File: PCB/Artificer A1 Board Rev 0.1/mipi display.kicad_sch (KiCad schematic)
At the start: 2 parts

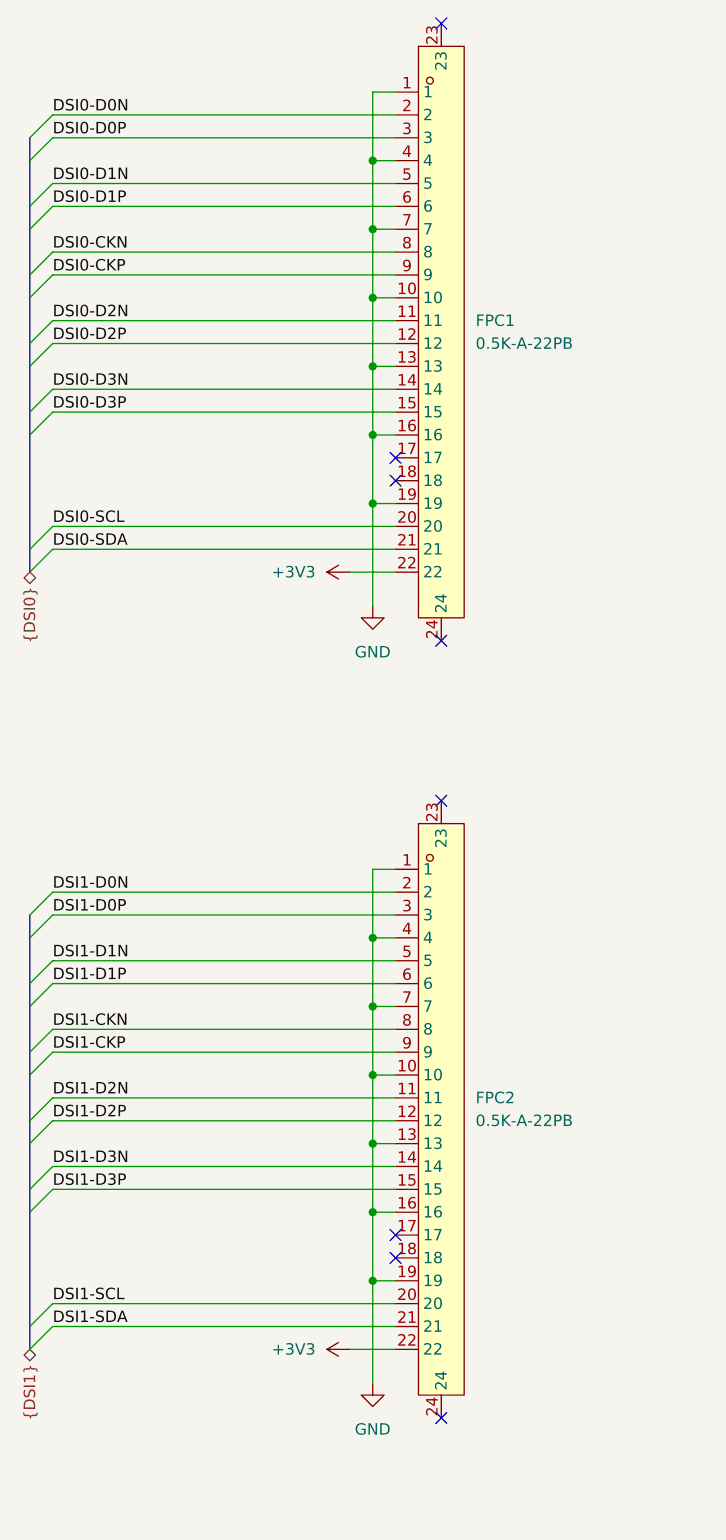
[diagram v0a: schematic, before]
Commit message: cleaned up, kicad 10 & usb c pd
migrated to Kicad 10,
added USB PD for power input
added capacitors inductors and resistor footprints
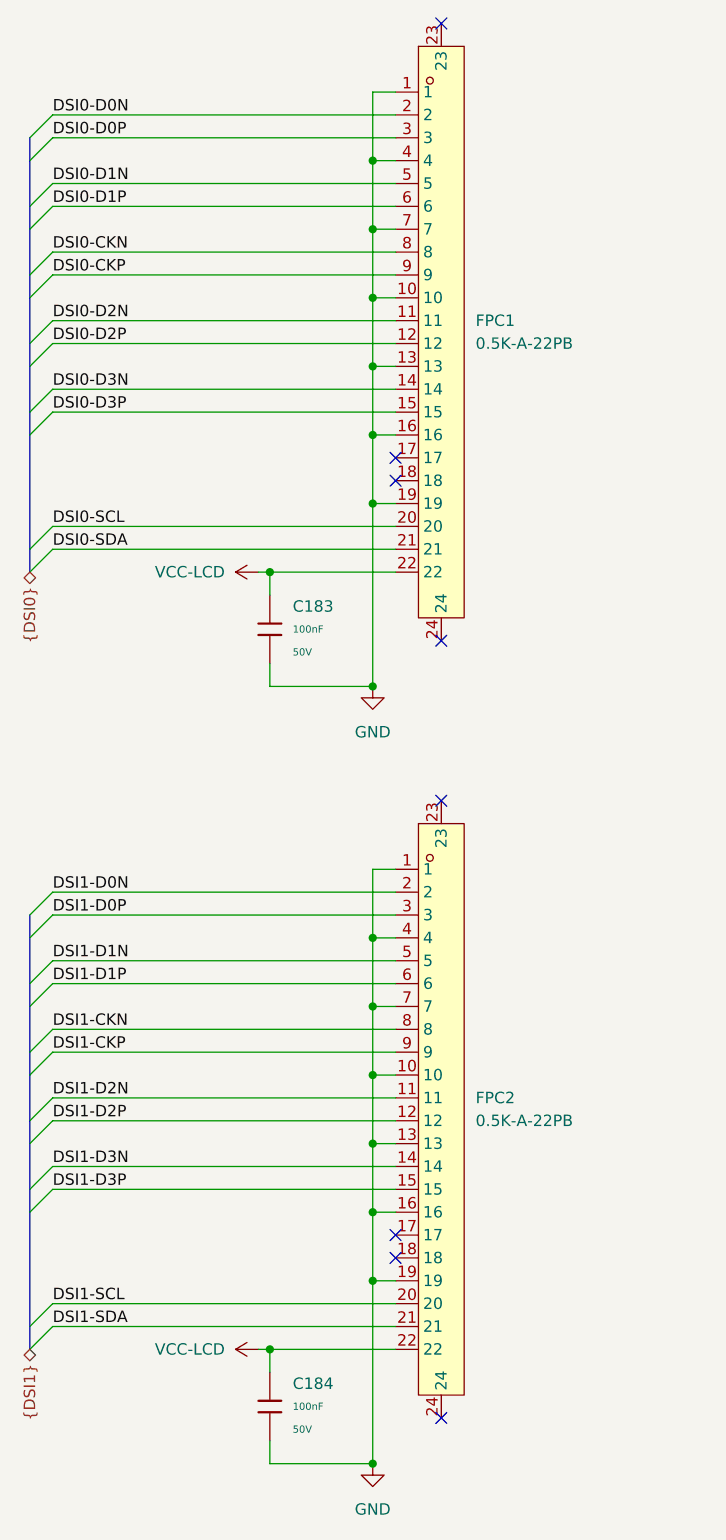
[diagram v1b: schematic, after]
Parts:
- added C183, C184: 100nF, PCM_JLCPCB:C_0402, symbol PCM_JLCPCB-Capacitors:0402,100nF,(2)
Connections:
- net GND: now also C183.2, C184.2
- net +3V3 renamed VCC-LCD
- net VCC-LCD: now also C183.1, C184.1

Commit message: placed all components
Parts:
- removed C183, C184: 100nF, PCM_JLCPCB:C_0402, symbol PCM_JLCPCB-Capacitors:0402,100nF,(2)
- added C159, C165: 100nF, Capacitor_SMD:C_0201_0603Metric, symbol Cap:JLCPCB_Lib_Blank_Cap
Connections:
- net GND: now also C159.1, C165.1
- net VCC-LCD: now also C159.2, C165.2

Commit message: started routing
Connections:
- net DSI0-SCL renamed Disp0-SCL
- net DSI0-SDA renamed Disp0-SDA
- net DSI1-SCL renamed Disp1-SCL
- net DSI1-SDA renamed Disp1-SDA
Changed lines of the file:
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@@
+	)
+	(bus_entry
+		(at 105.41 171.45)
+		(size 2.54 -2.54)
+		(stroke
+			(width 0)
+			(type default)
+		)
 	)
 	(bus_entry
@@
 	)
 	(bus_entry
+		(at 105.41 135.89)
+		(size 2.54 -2.54)
+		(stroke
+			(width 0)
+			(type default)
+		)
+	)
+	(bus_entry
+		(at 105.41 49.53)
+		(size 2.54 -2.54)
+		(stroke
+			(width 0)
+			(type default)
+		)
+	)
+	(bus_entry
+		(at 105.41 72.39)
+		(size 2.54 -2.54)
+		(stroke
+			(width 0)
+			(type default)
+		)
+	)
+	(bus_entry
+		(at 105.41 125.73)
+		(size 2.54 -2.54)
+		(stroke
+			(width 0)
+			(type default)
+		)
+	)
+	(bus_entry
+		(at 105.41 133.35)
+		(size 2.54 -2.54)
+		(stroke
+			(width 0)
+			(type default)
+		)
+	)
+	(bus_entry
 		(at 105.41 173.99)
 		(size 2.54 -2.54)
@@
 	)
 	(bus_entry
-		(at 105.41 135.89)
-		(size 2.54 -2.54)
-		(stroke
-			(width 0)
-			(type default)
-		)
-	)
-	(bus_entry
-		(at 105.41 49.53)
-		(size 2.54 -2.54)
-		(stroke
-			(width 0)
-			(type default)
-		)
-	)
-	(bus_entry
-		(at 105.41 72.39)
-		(size 2.54 -2.54)
-		(stroke
-			(width 0)
-			(type default)
-		)
-	)
-	(bus_entry
-		(at 105.41 125.73)
-		(size 2.54 -2.54)
-		(stroke
-			(width 0)
-			(type default)
-		)
-	)
-	(bus_entry
-		(at 105.41 133.35)
-		(size 2.54 -2.54)
-		(stroke
-			(width 0)
-			(type default)
-		)
-	)
-	(bus_entry
 		(at 105.41 85.09)
 		(size 2.54 -2.54)
@@
 	)
 	(bus_entry
-		(at 105.41 171.45)
-		(size 2.54 -2.54)
-		(stroke
-			(width 0)
-			(type default)
-		)
-	)
-	(bus_entry
 		(at 105.41 69.85)
 		(size 2.54 -2.54)
@@
 	(bus
 		(pts
-			(xy 105.41 158.75) (xy 105.41 171.45)
+			(xy 105.41 158.75) (xy 105.41 173.99)
 		)
 		(stroke
@@
 		(pts
 			(xy 143.51 166.37) (xy 143.51 186.69)
-		)
-		(stroke
-			(width 0)
-			(type default)
-		)
-	)
-	(bus
-		(pts
-			(xy 105.41 171.45) (xy 105.41 173.99)
 		)
 		(stroke
@@
 		)
 	)
-	(label "DSI0-SDA"
+	(label "Disp0-SDA"
 		(at 107.95 85.09 0)
 		(effects
@@
 		)
 	)
+	(label "Disp1-SDA"
+		(at 107.95 171.45 0)
+		(effects
+			(font
+				(size 1.27 1.27)
+			)
+			(justify left bottom)
+		)
+	)
 	(label "DSI0-D0N"
 		(at 107.95 36.83 0)
@@
 		)
 	)
+	(label "Disp1-SCL"
+		(at 107.95 168.91 0)
+		(effects
+			(font
+				(size 1.27 1.27)
+			)
+			(justify left bottom)
+		)
+	)
 	(label "DSI1-CKP"
 		(at 107.95 140.97 0)
@@
 		)
 	)
-	(label "DSI1-SDA"
-		(at 107.95 171.45 0)
-		(effects
-			(font
-				(size 1.27 1.27)
-			)
-			(justify left bottom)
-		)
-	)
 	(label "DSI0-D1P"
 		(at 107.95 46.99 0)
@@
 		)
 	)
-	(label "DSI1-SCL"
-		(at 107.95 168.91 0)
-		(effects
-			(font
-				(size 1.27 1.27)
-			)
-			(justify left bottom)
-		)
-	)
-	(label "DSI0-SCL"
+	(label "Disp0-SCL"
 		(at 107.95 82.55 0)
 		(effects

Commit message: more routing and decoupling
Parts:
- added R223, R224, R225, R226: 4.7k, Resistor_SMD:R_0201_0603Metric, symbol Cap:JLCPCB_Res_Custom
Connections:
- net Disp0-SCL: now also R223.2
- net Disp0-SDA: now also R224.2
- net Disp1-SCL: now also R225.2
- net Disp1-SDA: now also R226.2
- new net VCC3V3-CSI: R223.1, R224.1, R225.1, R226.1
